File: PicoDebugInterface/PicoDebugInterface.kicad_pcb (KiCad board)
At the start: 2 copper layers, 15.1 x 11.8 mm, 5 parts, among them J1 DebugCon, J2 SWDConnections, J3 I2C0_con, J4 I2C1_conn, J5 Conn_01x03_Female

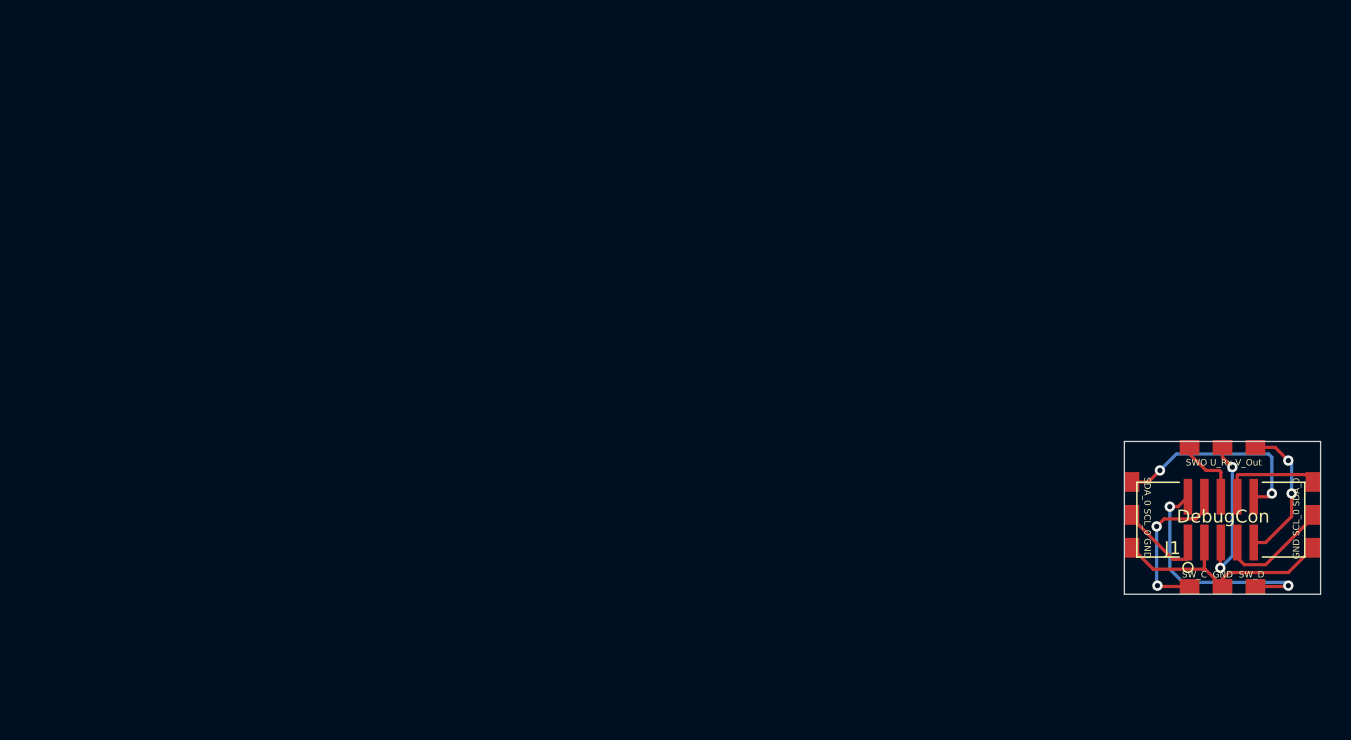
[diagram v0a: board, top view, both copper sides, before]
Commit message: pushed fix for the connector so it a staight through cable
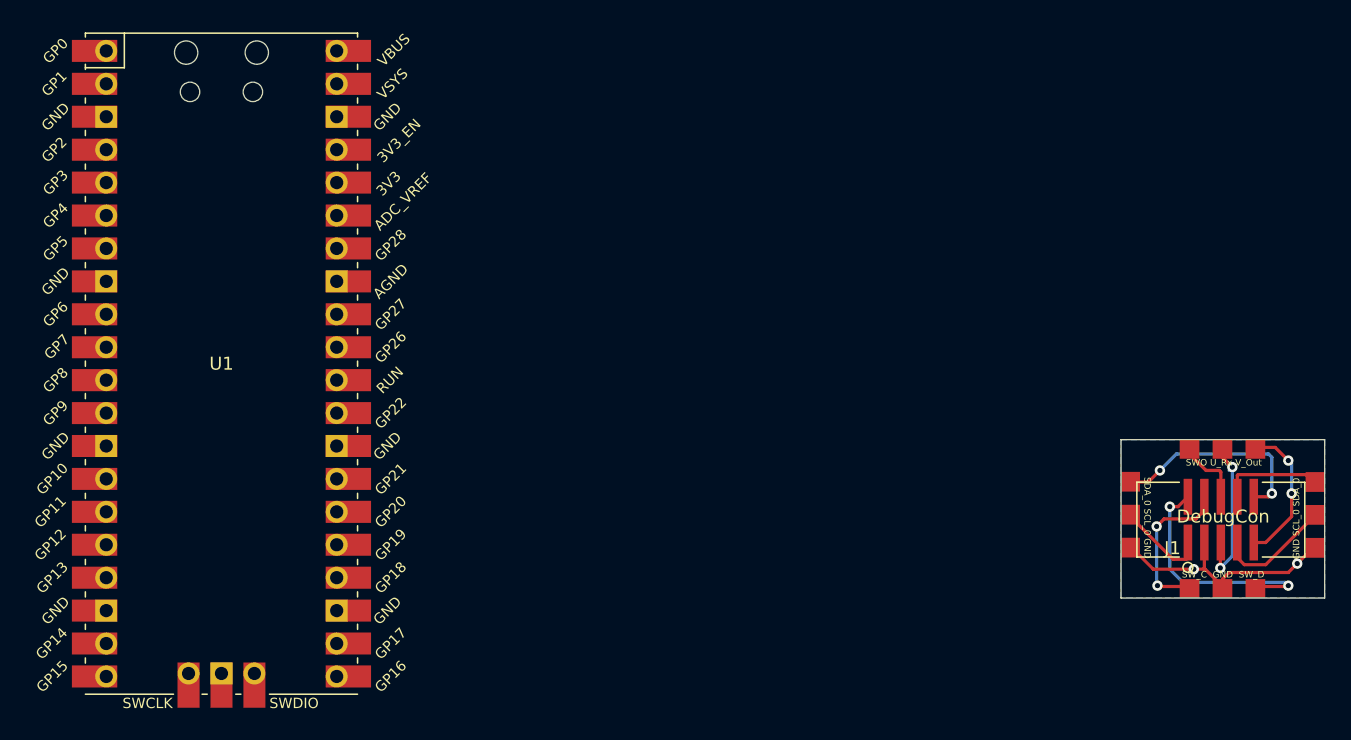
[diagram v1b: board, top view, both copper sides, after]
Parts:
- added U1: Pico, RP-Pico Libraries:RPi_Pico_SMD_TH, F.Cu at (51.5, 49.9)
- moved J3 0.25 mm to (121.0, 61.6)
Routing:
- net GND: vias 0 -> 2
- added copper zone on B.Cu, net GND
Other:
- board size 15.1 x 11.8 mm -> 15.7 x 12.2 mm
